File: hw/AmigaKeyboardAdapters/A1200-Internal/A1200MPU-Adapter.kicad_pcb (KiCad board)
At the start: 2 copper layers, 30.5 x 31.1 mm, 8 parts, among them P1 Conn_02x03_Odd_Even, U1 A1200U13_REV_PLCC44

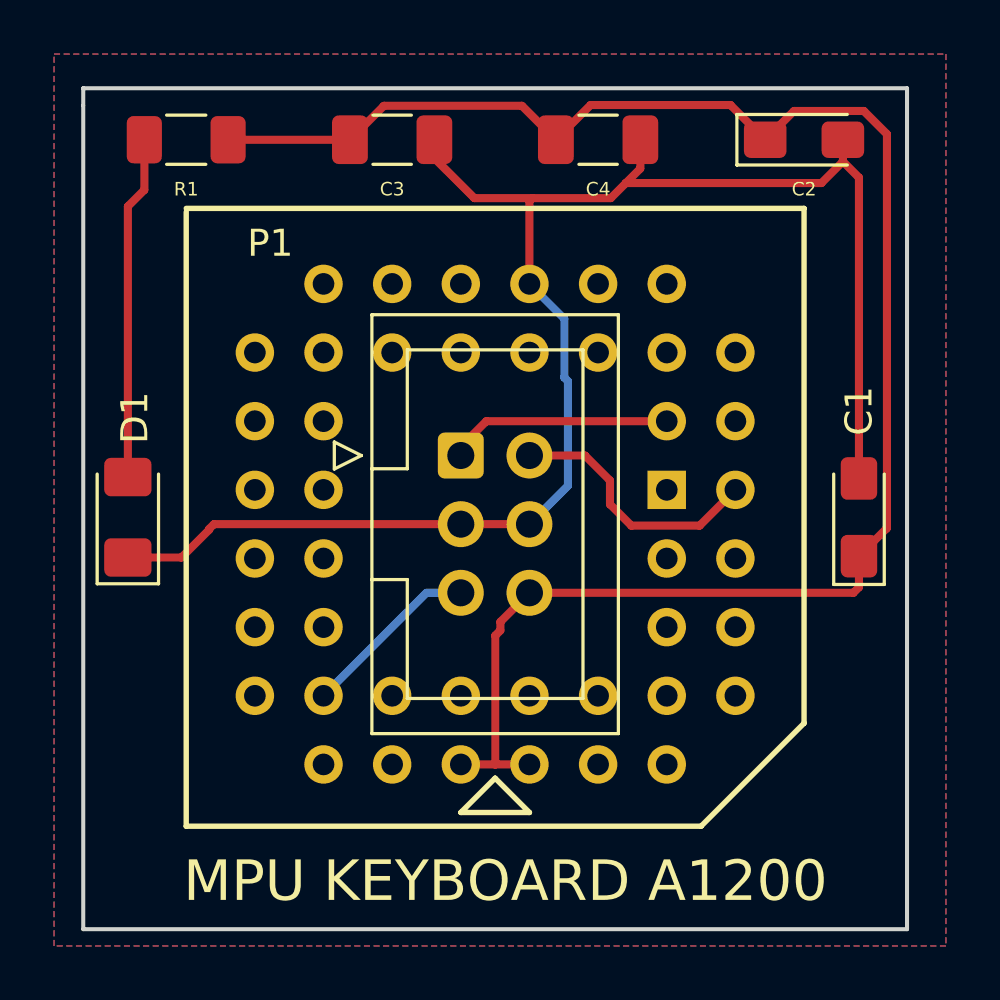
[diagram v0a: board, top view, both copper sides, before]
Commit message: Updated from Library. /IRQ is not tied at VCC anymore.
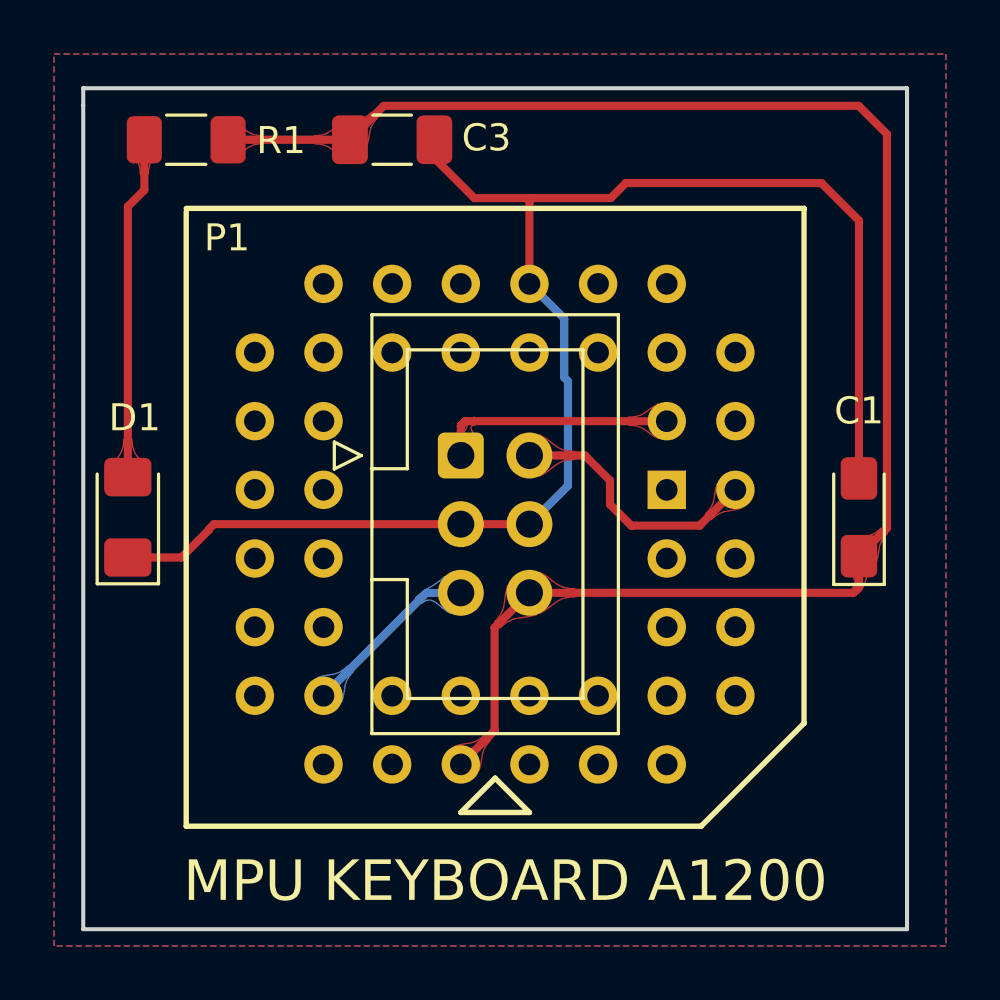
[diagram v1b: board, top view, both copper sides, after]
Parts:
- removed C2: 10uF, Capacitor_Tantalum_SMD:CP_EIA-3216-12_Kemet-S_Pad1.58x1.35mm_HandSolder
- removed C4: 100nF, Capacitor_SMD:C_1206_3216Metric_Pad1.33x1.80mm_HandSolder
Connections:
- U1 pad 11: VCC5V -> Net-(U1-Pad11)
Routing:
- net GND: track 61.1 -> 56.4 mm
- net VCC5V: track 66.2 -> 62.2 mm
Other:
- board text added: "RBL005.02"
- board text added: "designed by R.G.2018/2022/2026"
- board text removed: "RBL005.01"
- board text removed: "designed by R.G.2018/2022"
